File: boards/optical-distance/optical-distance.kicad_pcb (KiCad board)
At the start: 2 copper layers, 23 x 19.5 mm, 7 parts, among them J1 CONN_02X03, M3 MountingHole_3.2mm_M3, U1 DS9638

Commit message: [docs] export all board layouts
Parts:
- moved J1 130.9 mm to (62.2, 43.2)
- moved M3 130.9 mm to (68.9, 37.0)
- moved M3 130.9 mm to (68.9, 51.9)
- moved C1 130.9 mm to (63.5, 49.9)
- moved E1 130.9 mm to (65.4, 44.5)
- moved REF** 130.9 mm to (62.9, 37.0)
- moved U1 130.9 mm to (59.1, 50.8)

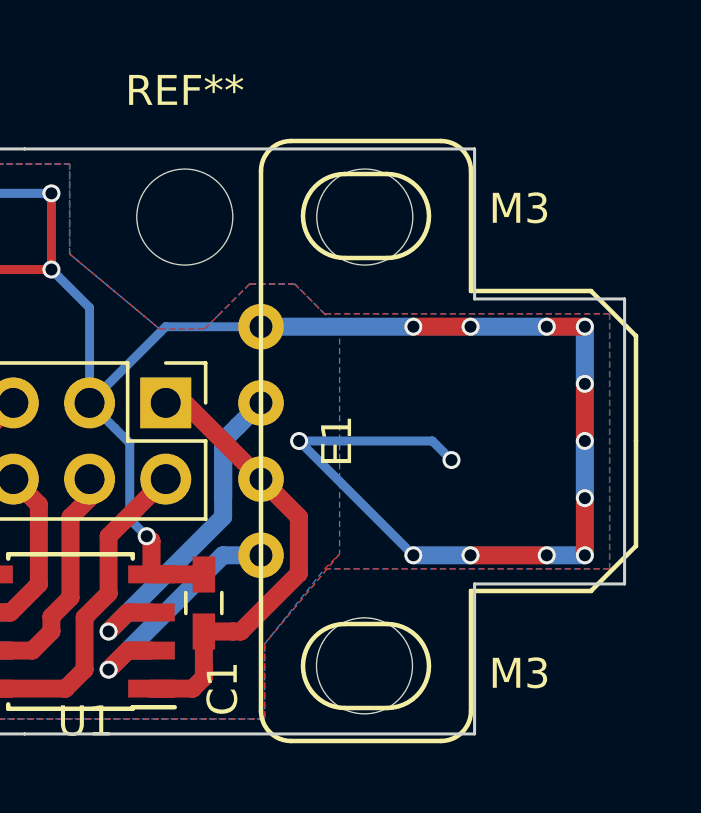
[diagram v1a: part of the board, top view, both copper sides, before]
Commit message: fix/heds: updated the footprint of the heds9731#X50
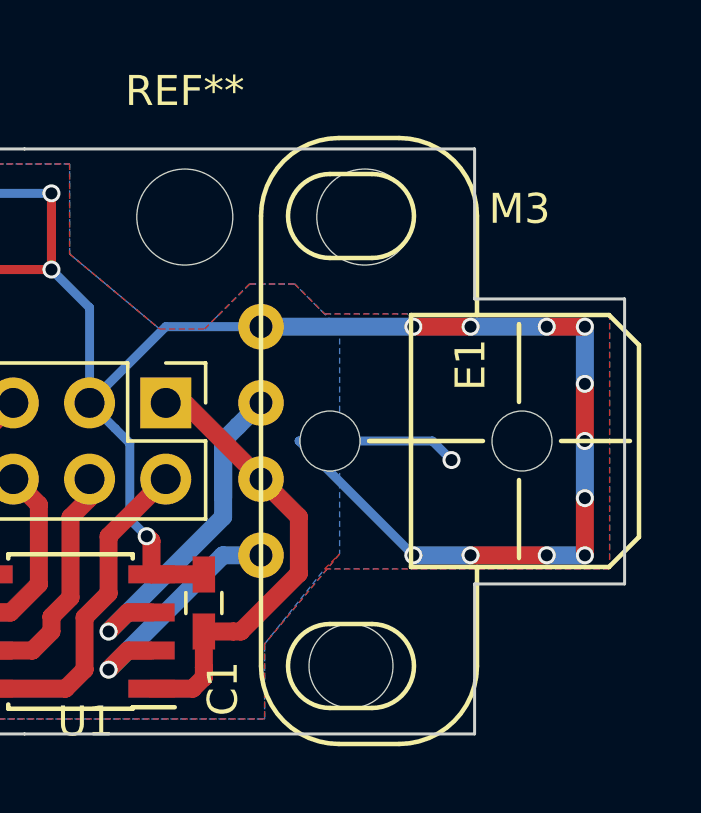
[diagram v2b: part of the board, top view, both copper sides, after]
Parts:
- removed the M3 at (68.9, 51.9)
- E1: footprint rchojetzki-optical-distance:HEDS-973X#X50 -> rchojetzki-optical-distance:HEDS-9731#X50
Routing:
- net /GND: vias 19 -> 18
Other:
- board text added: "optical-dis- tance board"
- board text added: "rexus-viper ©rchojetzki"
- board text removed: "rexus-viper optical-dis- tance board ©rchojetzki"
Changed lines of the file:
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@@
     (links 12)
     (no_connects 0)
-    (area 170.782857 89.025 206.85 120.200001)
+    (area 54.474999 34.664999 77.575001 54.265001)
     (thickness 1.6)
-    (drawings 19)
-    (tracks 96)
+    (drawings 20)
+    (tracks 95)
     (zones 0)
-    (modules 7)
+    (modules 6)
     (nets 9)
   )
@@
     (add_net "Net-(E1-Pad4)")
   )
-  (module rchojetzki-optical-distance:HEDS-973X#X50 (layer F.Cu)
+  (module rchojetzki-optical-distance:HEDS-9731#X50 (layer F.Cu)
     (at 65.405 44.45 90)
-    (fp_text reference E1 (at 0 2.54 90) (layer F.SilkS)
-      (effects (font (size 1 1) (thickness 0.15)))
-    )
-    (fp_text value HEDS-9731#15X (at 0.235 8.12 90) (layer F.Fab)
-      (effects (font (size 1 1) (thickness 0.15)))
-    )
-    (fp_line (start -9 7) (end -5 7) (layer F.SilkS) (width 0.15))
-    (fp_line (start -10 1) (end -10 6) (layer F.SilkS) (width 0.15))
-    (fp_line (start 9 0) (end -9 0) (layer F.SilkS) (width 0.15))
-    (fp_line (start 10 6) (end 10 1) (layer F.SilkS) (width 0.15))
-    (fp_line (start 9 7) (end 5 7) (layer F.SilkS) (width 0.15))
-    (fp_arc (start -9 6) (end -9 7) (angle 90) (layer F.SilkS) (width 0.15))
-    (fp_arc (start -9 1) (end -10 1) (angle 90) (layer F.SilkS) (width 0.15))
-    (fp_arc (start 9 6) (end 10 6) (angle 90) (layer F.SilkS) (width 0.15))
-    (fp_arc (start 9 1) (end 9 0) (angle 90) (layer F.SilkS) (width 0.15))
-    (fp_line (start -8.9 2.8) (end -8.9 4.2) (layer F.SilkS) (width 0.15))
-    (fp_line (start -6.1 2.8) (end -6.1 4.2) (layer F.SilkS) (width 0.15))
-    (fp_arc (start -7.5 4.2) (end -8.9 4.2) (angle -180) (layer F.SilkS) (width 0.15))
-    (fp_arc (start -7.5 2.8) (end -8.9 2.8) (angle 180) (layer F.SilkS) (width 0.15))
-    (fp_line (start 6.1 4.2) (end 6.1 2.8) (layer F.SilkS) (width 0.15))
-    (fp_line (start 8.9 2.8) (end 8.9 4.2) (layer F.SilkS) (width 0.15))
-    (fp_arc (start 7.5 2.8) (end 8.9 2.8) (angle -180) (layer F.SilkS) (width 0.15))
-    (fp_arc (start 7.5 4.2) (end 8.9 4.2) (angle 180) (layer F.SilkS) (width 0.15))
-    (fp_line (start -5 11) (end -5 7) (layer F.SilkS) (width 0.15))
-    (fp_line (start -3.5 12.5) (end -5 11) (layer F.SilkS) (width 0.15))
-    (fp_line (start 0 12.5) (end -3.5 12.5) (layer F.SilkS) (width 0.15))
-    (fp_line (start 5 11) (end 5 7) (layer F.SilkS) (width 0.15))
-    (fp_line (start 3.5 12.5) (end 5 11) (layer F.SilkS) (width 0.15))
-    (fp_line (start 0 12.5) (end 3.5 12.5) (layer F.SilkS) (width 0.15))
+    (fp_text reference E1 (at 2.54 6.985 90) (layer F.SilkS)
+      (effects (font (size 1 1) (thickness 0.15)))
+    )
+    (fp_text value HEDS-9731#15X (at 0 -2 90) (layer F.Fab)
+      (effects (font (size 1 1) (thickness 0.15)))
+    )
+    (fp_line (start 4.2 7.2) (end 4.2 5) (layer F.SilkS) (width 0.15))
+    (fp_line (start -4.2 5) (end -4.2 7.2) (layer F.SilkS) (width 0.15))
+    (fp_line (start -4.2 5) (end 4.2 5) (layer F.SilkS) (width 0.15))
+    (fp_line (start -3.9 8.6) (end -1.3 8.6) (layer F.SilkS) (width 0.15))
+    (fp_line (start 0 10) (end 0 12.3) (layer F.SilkS) (width 0.15))
+    (fp_line (start -7.5 0) (end 7.5 0) (layer F.SilkS) (width 0.15))
+    (fp_line (start -7.5 7.2) (end -4.2 7.2) (layer F.SilkS) (width 0.15))
+    (fp_line (start 10.1 2.6) (end 10.1 4.6) (layer F.SilkS) (width 0.15))
+    (fp_arc (start -7.5 2.6) (end -10.1 2.6) (angle 90) (layer F.SilkS) (width 0.15))
+    (fp_arc (start 7.5 4.6) (end 10.1 4.6) (angle 90) (layer F.SilkS) (width 0.15))
+    (fp_arc (start 7.5 2.6) (end 7.5 0) (angle 90) (layer F.SilkS) (width 0.15))
+    (fp_line (start -8.9 2.3) (end -8.9 3.7) (layer F.SilkS) (width 0.15))
+    (fp_line (start -6.1 2.3) (end -6.1 3.7) (layer F.SilkS) (width 0.15))
+    (fp_arc (start -7.5 3.7) (end -8.9 3.7) (angle -180) (layer F.SilkS) (width 0.15))
+    (fp_arc (start -7.5 2.3) (end -8.9 2.3) (angle 180) (layer F.SilkS) (width 0.15))
+    (fp_line (start 6.1 3.7) (end 6.1 2.3) (layer F.SilkS) (width 0.15))
+    (fp_line (start 8.9 2.3) (end 8.9 3.7) (layer F.SilkS) (width 0.15))
+    (fp_arc (start 7.5 2.3) (end 8.9 2.3) (angle -180) (layer F.SilkS) (width 0.15))
+    (fp_arc (start 7.5 3.7) (end 8.9 3.7) (angle 180) (layer F.SilkS) (width 0.15))
+    (fp_line (start -4.2 11.6) (end -4.2 7.2) (layer F.SilkS) (width 0.15))
+    (fp_line (start -3.2 12.6) (end -4.2 11.6) (layer F.SilkS) (width 0.15))
+    (fp_line (start 3.2 12.6) (end -3.2 12.6) (layer F.SilkS) (width 0.15))
+    (fp_line (start 3.2 12.6) (end 4.2 11.6) (layer F.SilkS) (width 0.15))
+    (fp_arc (start -7.5 4.6) (end -7.5 7.2) (angle 90) (layer F.SilkS) (width 0.15))
+    (fp_line (start -10.1 2.6) (end -10.1 4.6) (layer F.SilkS) (width 0.15))
+    (fp_line (start 7.5 7.2) (end 4.2 7.2) (layer F.SilkS) (width 0.15))
+    (fp_line (start 4.2 11.6) (end 4.2 7.2) (layer F.SilkS) (width 0.15))
+    (fp_line (start 0 7.4) (end 0 3.6) (layer F.SilkS) (width 0.15))
+    (fp_line (start 3.9 8.6) (end 1.3 8.6) (layer F.SilkS) (width 0.15))
     (pad 1 thru_hole circle (at 3.81 0 90) (size 1.524 1.524) (drill 0.762) (layers *.Cu *.Mask)
       (net 4 /GND))
@@
     (pad 4 thru_hole circle (at -3.81 0 90) (size 1.524 1.524) (drill 0.762) (layers *.Cu *.Mask)
       (net 2 "Net-(E1-Pad4)"))
+    (pad "" np_thru_hole circle (at 0 2.3 90) (size 2 2) (drill 2) (layers *.Cu *.Mask)
+      (solder_mask_margin 0.1) (solder_paste_margin 0.1) (clearance 0.1))
+    (pad "" np_thru_hole circle (at 0 8.7 90) (size 2 2) (drill 2) (layers *.Cu *.Mask)
+      (solder_mask_margin 0.1) (solder_paste_margin 0.1) (clearance 0.1))
+    (pad "" np_thru_hole circle (at -7.5 3 90) (size 2.8 2.8) (drill 2.8) (layers *.Cu *.Mask)
+      (solder_mask_margin 0.1) (solder_paste_margin 0.1) (clearance 0.1))
     (model F:/Richard/dev/viper/elektronik_repo/rexus-viper-elektronik/boards/optical-distance/rchojetzki-optical-distance.pretty/HEDS-973X#X50.wrl
       (at (xyz 0 0 0))
@@
     (pad 1 np_thru_hole circle (at 0 0) (size 3.2 3.2) (drill 3.2) (layers *.Cu *.Mask))
   )
-  (module Mounting_Holes:MountingHole_3.2mm_M3 (layer F.Cu)
-    (at 68.855 51.945)
-    (descr "Mounting Hole 3.2mm, no annular, M3")
-    (tags "mounting hole 3.2mm no annular m3")
-    (fp_text reference M3 (at 5.17 0.27) (layer F.SilkS)
-      (effects (font (size 1 1) (thickness 0.15)))
-    )
-    (fp_text value MountingHole_3.2mm_M3 (at 6.67 4.27) (layer F.Fab)
-      (effects (font (size 1 1) (thickness 0.15)))
-    )
-    (fp_circle (center 0 0) (end 3.2 0) (layer Cmts.User) (width 0.15))
-    (fp_circle (center 0 0) (end 3.45 0) (layer F.CrtYd) (width 0.05))
-    (pad 1 np_thru_hole circle (at 0 0) (size 3.2 3.2) (drill 3.2) (layers *.Cu *.Mask))
-  )
   (module Capacitors_SMD:C_0603_HandSoldering (layer F.Cu)
     (at 63.5 49.85 90)
@@
     (pad 1 np_thru_hole circle (at 0 0) (size 3.2 3.2) (drill 3.2) (layers *.Cu *.Mask))
   )
+  (gr_text "optical-dis-\ntance board" (at 60.325 51.435) (layer B.SilkS)
+    (effects (font (size 1 1) (thickness 0.2)) (justify mirror))
+  )
   (gr_text B* (at 57.15 40.64 270) (layer B.SilkS)
     (effects (font (size 1.5 1.5) (thickness 0.3)) (justify mirror))
@@
   (gr_line (start 54.525 34.715) (end 54.525 54.215) (layer Edge.Cuts) (width 0.1))
   (gr_line (start 57.525 34.715) (end 54.525 34.715) (layer Edge.Cuts) (width 0.1))
-  (gr_text "rexus-viper\noptical-dis-\ntance board\n©rchojetzki" (at 71.755 44.45) (layer B.SilkS)
+  (gr_text "rexus-viper\n\n\n©rchojetzki" (at 71.755 44.45) (layer B.SilkS)
     (effects (font (size 1 1) (thickness 0.2)) (justify mirror))
   )
@@
   (via (at 71.755 45.085) (size 0.6) (drill 0.4) (layers F.Cu B.Cu) (net 4))
   (segment (start 70.485 48.26) (end 66.675 44.45) (width 0.3) (layer B.Cu) (net 4))
-  (via (at 66.675 44.45) (size 0.6) (drill 0.4) (layers F.Cu B.Cu) (net 4))
   (segment (start 58.42 36.195) (end 58.42 38.735) (width 0.3) (layer F.Cu) (net 4))
   (segment (start 55.88 36.195) (end 58.42 36.195) (width 0.3) (layer B.Cu) (net 4))

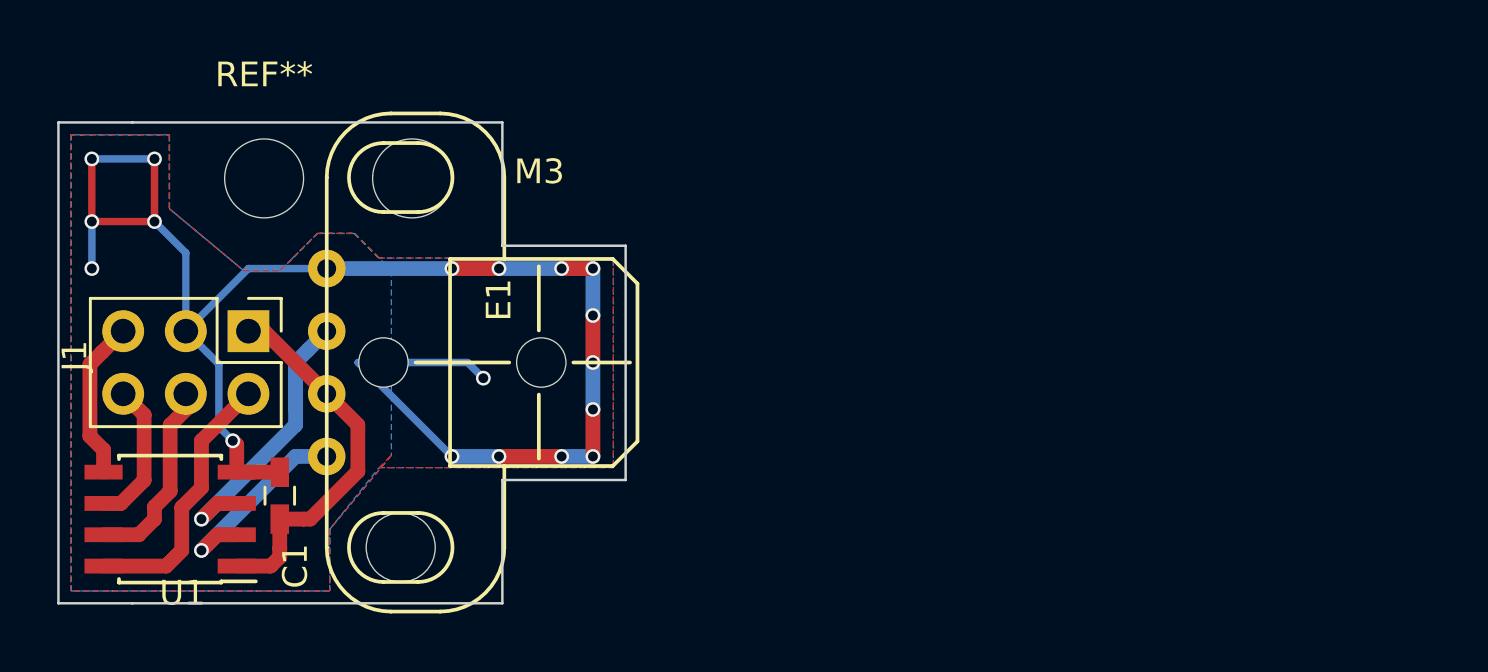
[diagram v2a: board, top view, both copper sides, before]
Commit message: boards/op_v3: changed complete layout to accomodete cable-slot
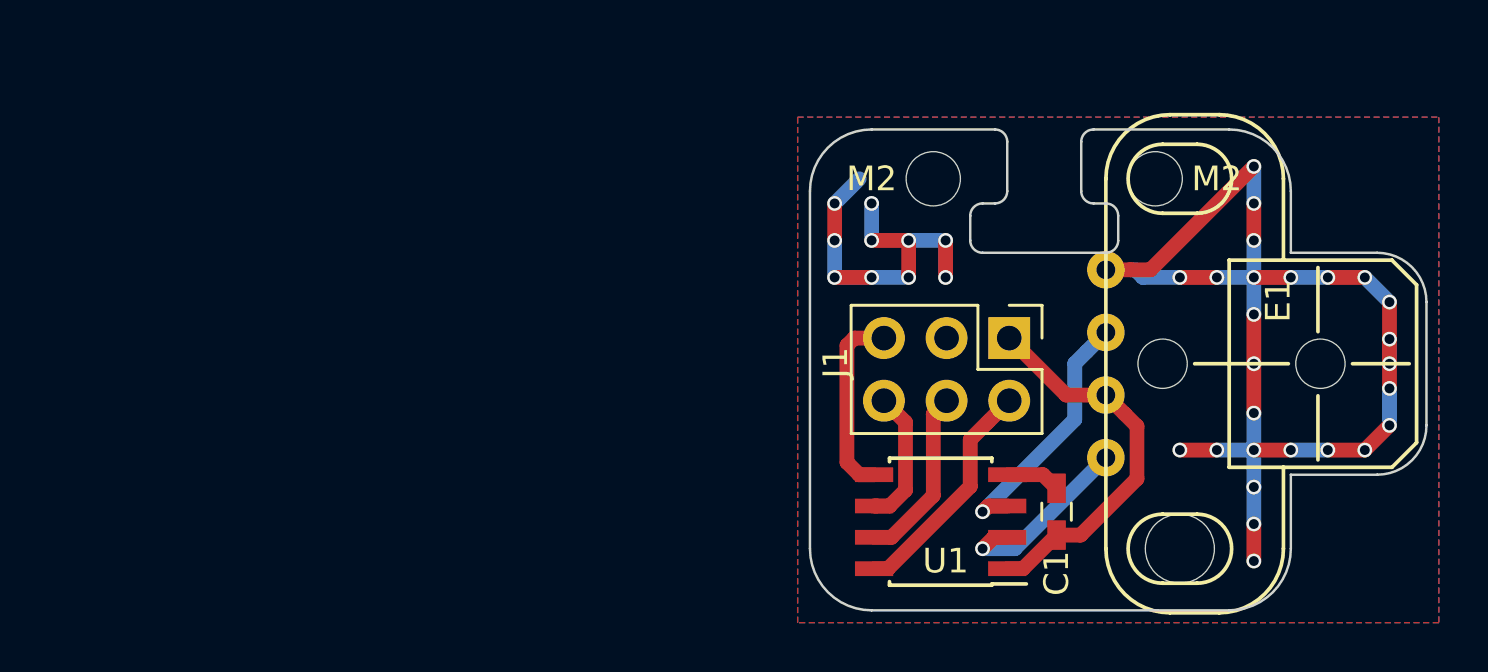
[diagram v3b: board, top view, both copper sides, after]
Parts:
- removed M3, REF**: MountingHole_3.2mm_M3, Mounting_Holes:MountingHole_3.2mm_M3
- added M2: MountingHole_2.2mm_M2, Mounting_Holes:MountingHole_2.2mm_M2, F.Cu at (99.0, 37.0)
- added M2: MountingHole_2.2mm_M2, Mounting_Holes:MountingHole_2.2mm_M2, F.Cu at (90.0, 37.0)
- moved E1 31.6 mm to (97.0, 44.5)
- moved C1 31.5 mm to (95.0, 50.5)
- moved U1 31.2 mm to (90.3, 50.9)
- moved J1 30.9 mm to (93.1, 43.5)
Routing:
- net (no net): track 0.00 -> 17.9 mm, vias 0 -> 10
- net /GND: track 67.0 -> 51.9 mm, vias 18 -> 26
- net Net-(E1-Pad2): track 13.3 -> 10.4 mm
- net /A: track 10.9 -> 9.41 mm
- net /B*: track 6.50 -> 7.67 mm
- net /A*: track 7.93 -> 7.17 mm
- net Net-(E1-Pad4): track 8.35 -> 7.72 mm
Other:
- board size 23 x 19.5 mm -> 25 x 19.5 mm
- board text added: "5V"
- board text added: "rev3"
- board text removed: "VCC"
